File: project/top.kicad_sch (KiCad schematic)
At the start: 11 parts, among them J1 IDC 2x8, U1 top, U2 mag

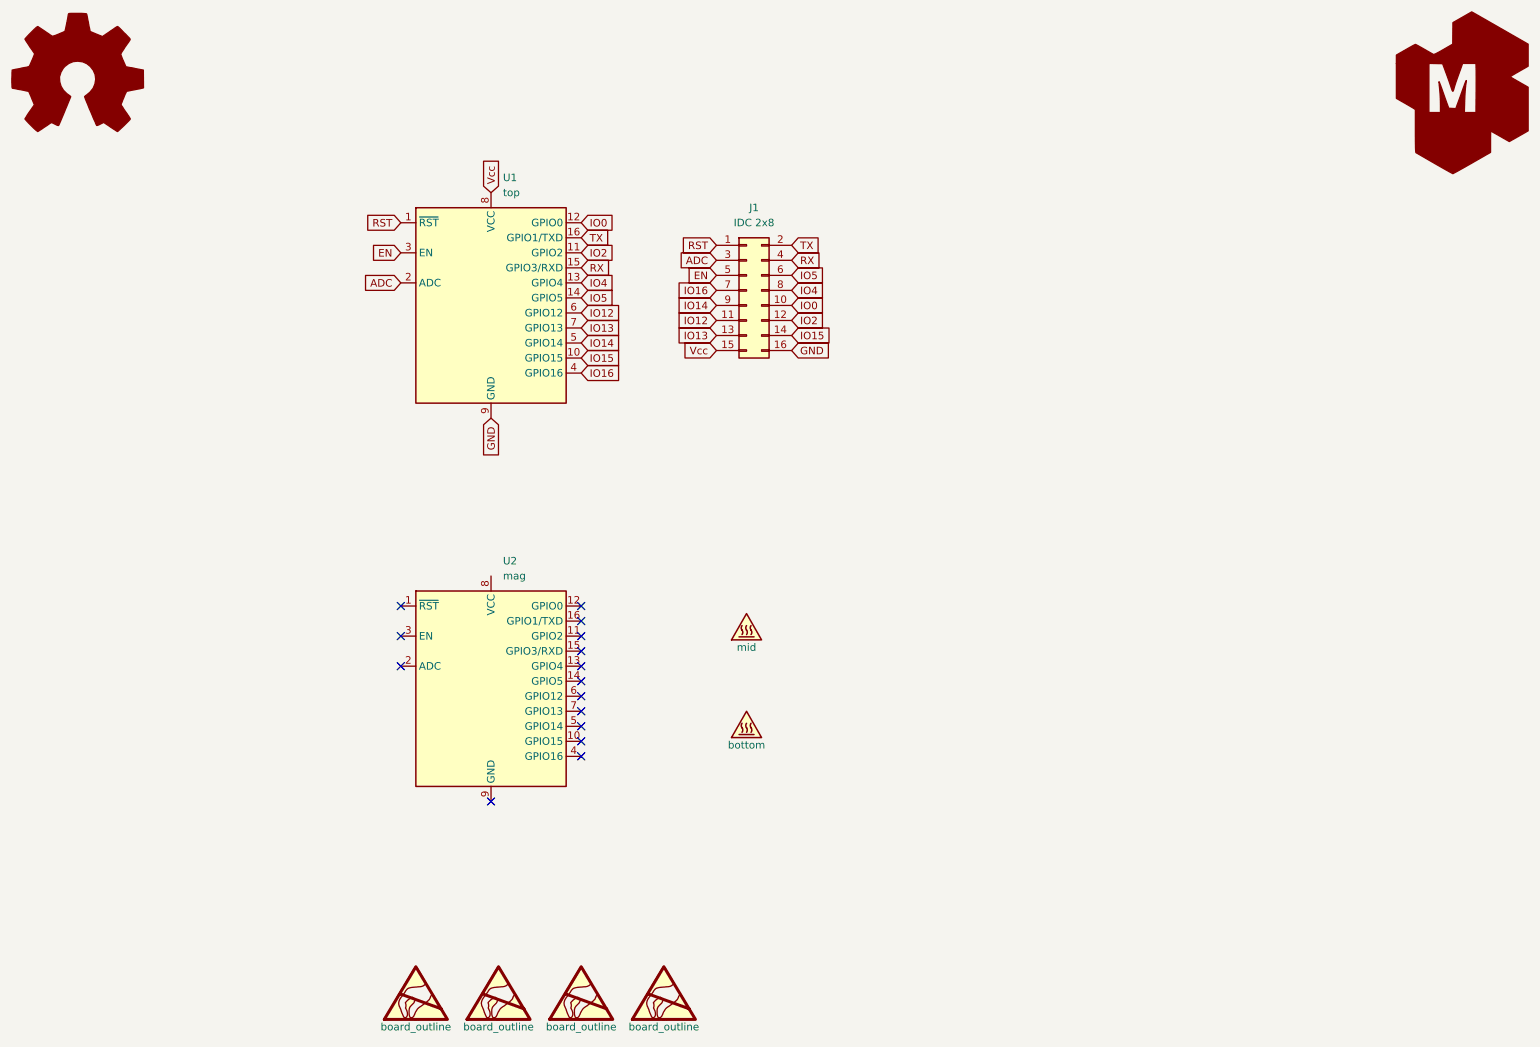
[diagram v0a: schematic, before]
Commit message: splitting boards into separate projects
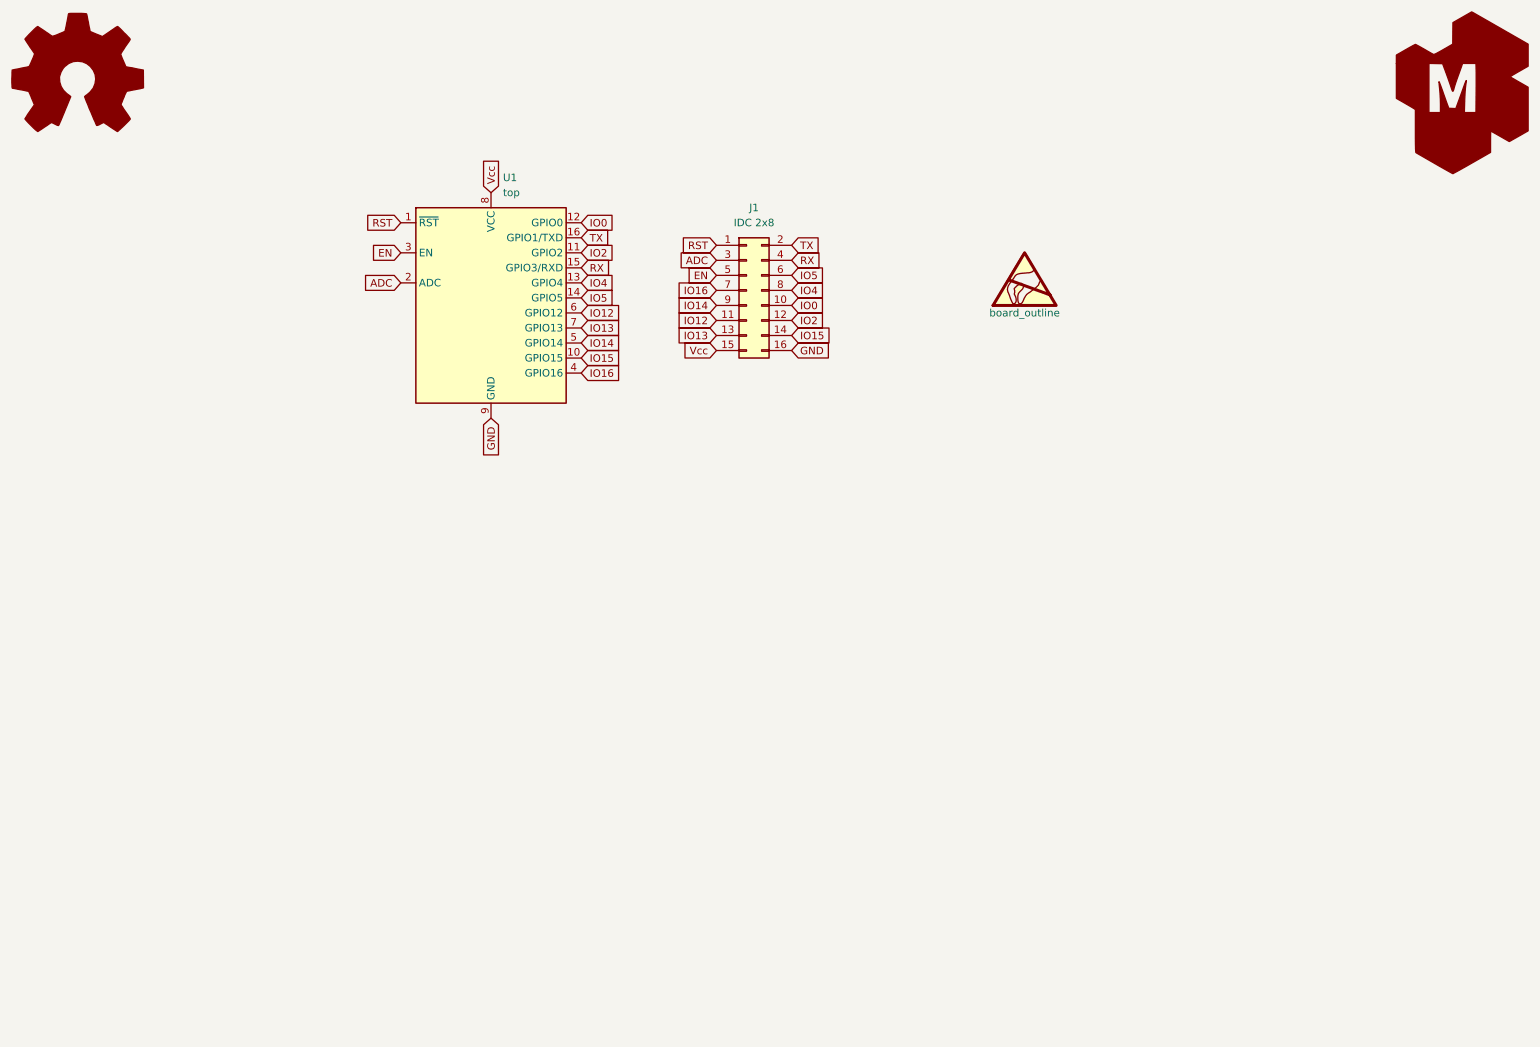
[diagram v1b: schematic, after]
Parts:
- removed SYM2, SYM3, SYM4: board_outline, -local:board, symbol Graphic:SYM_ESD_Large
- removed SYM5: mid, -local:esp-mid, symbol Graphic:SYM_Hot_Small
- removed SYM6: bottom, -local:esp-bottom, symbol Graphic:SYM_Hot_Small
- removed U2: mag, -local:esp-magnets, symbol RF_Module:ESP-07
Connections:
- no-connect marks 15 -> 0
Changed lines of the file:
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@@
     (company "makerspace.lt")
   )
-  (no_connect (at 115.57 121.92))
-  (no_connect (at 100.33 152.4))
-  (no_connect (at 115.57 124.46))
-  (no_connect (at 115.57 139.7))
-  (no_connect (at 115.57 137.16))
-  (no_connect (at 115.57 142.24))
-  (no_connect (at 85.09 124.46))
-  (no_connect (at 85.09 129.54))
-  (no_connect (at 115.57 119.38))
-  (no_connect (at 115.57 132.08))
-  (no_connect (at 115.57 127))
-  (no_connect (at 115.57 129.54))
-  (no_connect (at 115.57 134.62))
-  (no_connect (at 115.57 144.78))
-  (no_connect (at 85.09 119.38))
   (global_label "IO0" (shape input) (at 151.13 68.58 0) (fields_autoplaced)
     (effects (font (size 1.27 1.27)) (justify left))
@@
     (property "Intersheet References" "${INTERSHEET_REFS}" (id 0) (at 131.6626 73.7394 0)
       (effects (font (size 1.27 1.27)) (justify right) hide)
-    )
-  )
-  (symbol (lib_id "Graphic:SYM_ESD_Large") (at 101.6 184.15 0) (unit 1)
-    (in_bom no) (on_board yes) (fields_autoplaced)
-    (property "Reference" "SYM2" (id 0) (at 101.6 179.07 0)
-      (effects (font (size 1.27 1.27)) hide)
-    )
-    (property "Value" "board_outline" (id 1) (at 101.6 190.5 0))
-    (property "Footprint" "-local:board" (id 2) (at 101.473 184.912 0)
-      (effects (font (size 1.27 1.27)) hide)
-    )
-    (property "Datasheet" "~" (id 3) (at 101.473 184.912 0)
-      (effects (font (size 1.27 1.27)) hide)
     )
   )
@@
     (pin "9")
   )
-  (symbol (lib_id "Graphic:SYM_ESD_Large") (at 129.54 184.15 0) (unit 1)
+  (symbol (lib_id "Graphic:SYM_ESD_Large") (at 190.5 63.5 0) (unit 1)
     (in_bom no) (on_board yes) (fields_autoplaced)
-    (property "Reference" "SYM4" (id 0) (at 129.54 179.07 0)
-      (effects (font (size 1.27 1.27)) hide)
-    )
-    (property "Value" "board_outline" (id 1) (at 129.54 190.5 0))
-    (property "Footprint" "-local:board" (id 2) (at 129.413 184.912 0)
-      (effects (font (size 1.27 1.27)) hide)
-    )
-    (property "Datasheet" "~" (id 3) (at 129.413 184.912 0)
-      (effects (font (size 1.27 1.27)) hide)
-    )
-  )
-  (symbol (lib_id "Graphic:SYM_ESD_Large") (at 87.63 184.15 0) (unit 1)
+    (property "Reference" "SYM1" (id 0) (at 190.5 58.42 0)
+      (effects (font (size 1.27 1.27)) hide)
+    )
+    (property "Value" "board_outline" (id 1) (at 190.5 69.85 0))
+    (property "Footprint" "-local:board" (id 2) (at 190.373 64.262 0)
+      (effects (font (size 1.27 1.27)) hide)
+    )
+    (property "Datasheet" "~" (id 3) (at 190.373 64.262 0)
+      (effects (font (size 1.27 1.27)) hide)
+    )
+  )
+  (symbol (lib_id "RF_Module:ESP-07") (at 100.33 69.85 0) (unit 1)
     (in_bom no) (on_board yes) (fields_autoplaced)
-    (property "Reference" "SYM1" (id 0) (at 87.63 179.07 0)
-      (effects (font (size 1.27 1.27)) hide)
-    )
-    (property "Value" "board_outline" (id 1) (at 87.63 190.5 0))
-    (property "Footprint" "-local:board" (id 2) (at 87.503 184.912 0)
-      (effects (font (size 1.27 1.27)) hide)
-    )
-    (property "Datasheet" "~" (id 3) (at 87.503 184.912 0)
-      (effects (font (size 1.27 1.27)) hide)
-    )
-  )
-  (symbol (lib_id "RF_Module:ESP-07") (at 100.33 134.62 0) (unit 1)
-    (in_bom no) (on_board yes) (fields_autoplaced)
-    (property "Reference" "U2" (id 0) (at 102.3494 111.76 0)
+    (property "Reference" "U1" (id 0) (at 102.3494 46.99 0)
       (effects (font (size 1.27 1.27)) (justify left))
     )
-    (property "Value" "mag" (id 1) (at 102.3494 114.3 0)
+    (property "Value" "top" (id 1) (at 102.3494 49.53 0)
       (effects (font (size 1.27 1.27)) (justify left))
     )
-    (property "Footprint" "-local:esp-magnets" (id 2) (at 100.33 134.62 0)
-      (effects (font (size 1.27 1.27)) hide)
-    )
-    (property "Datasheet" "" (id 3) (at 91.44 132.08 0)
+    (property "Footprint" "-local:esp-top" (id 2) (at 100.33 69.85 0)
+      (effects (font (size 1.27 1.27)) hide)
+    )
+    (property "Datasheet" "" (id 3) (at 91.44 67.31 0)
       (effects (font (size 1.27 1.27)) hide)
     )
@@
     (pin "9")
   )
-  (symbol (lib_id "RF_Module:ESP-07") (at 100.33 69.85 0) (unit 1)
-    (in_bom no) (on_board yes) (fields_autoplaced)
-    (property "Reference" "U1" (id 0) (at 102.3494 46.99 0)
-      (effects (font (size 1.27 1.27)) (justify left))
-    )
-    (property "Value" "top" (id 1) (at 102.3494 49.53 0)
-      (effects (font (size 1.27 1.27)) (justify left))
-    )
-    (property "Footprint" "-local:esp-top" (id 2) (at 100.33 69.85 0)
-      (effects (font (size 1.27 1.27)) hide)
-    )
-    (property "Datasheet" "" (id 3) (at 91.44 67.31 0)
-      (effects (font (size 1.27 1.27)) hide)
-    )
-    (pin "1")
-    (pin "10")
-    (pin "11")
-    (pin "12")
-    (pin "13")
-    (pin "14")
-    (pin "15")
-    (pin "16")
-    (pin "2")
-    (pin "3")
-    (pin "4")
-    (pin "5")
-    (pin "6")
-    (pin "7")
-    (pin "8")
-    (pin "9")
-  )
   (symbol (lib_id "-local:LOGO_KMS") (at 262.89 31.75 0) (unit 1)
     (in_bom no) (on_board yes) (fields_autoplaced)
@@
     )
   )
-  (symbol (lib_id "Graphic:SYM_Hot_Small") (at 143.51 139.7 0) (unit 1)
-    (in_bom no) (on_board yes) (fields_autoplaced)
-    (property "Reference" "SYM6" (id 0) (at 143.51 136.144 0)
-      (effects (font (size 1.27 1.27)) hide)
-    )
-    (property "Value" "bottom" (id 1) (at 143.51 142.875 0))
-    (property "Footprint" "-local:esp-bottom" (id 2) (at 143.51 144.145 0)
-      (effects (font (size 1.27 1.27)) hide)
-    )
-    (property "Datasheet" "~" (id 3) (at 144.272 144.78 0)
-      (effects (font (size 1.27 1.27)) hide)
-    )
-  )
-  (symbol (lib_id "Graphic:SYM_ESD_Large") (at 115.57 184.15 0) (unit 1)
-    (in_bom no) (on_board yes) (fields_autoplaced)
-    (property "Reference" "SYM3" (id 0) (at 115.57 179.07 0)
-      (effects (font (size 1.27 1.27)) hide)
-    )
-    (property "Value" "board_outline" (id 1) (at 115.57 190.5 0))
-    (property "Footprint" "-local:board" (id 2) (at 115.443 184.912 0)
-      (effects (font (size 1.27 1.27)) hide)
-    )
-    (property "Datasheet" "~" (id 3) (at 115.443 184.912 0)
-      (effects (font (size 1.27 1.27)) hide)
-    )
-  )
-  (symbol (lib_id "Graphic:SYM_Hot_Small") (at 143.51 123.19 0) (unit 1)
-    (in_bom no) (on_board yes) (fields_autoplaced)
-    (property "Reference" "SYM5" (id 0) (at 143.51 119.634 0)
-      (effects (font (size 1.27 1.27)) hide)
-    )
-    (property "Value" "mid" (id 1) (at 143.51 126.365 0))
-    (property "Footprint" "-local:esp-mid" (id 2) (at 143.51 127.635 0)
-      (effects (font (size 1.27 1.27)) hide)
-    )
-    (property "Datasheet" "~" (id 3) (at 144.272 128.27 0)
-      (effects (font (size 1.27 1.27)) hide)
-    )
-  )
   (symbol (lib_id "Graphic:Logo_Open_Hardware_Large") (at 30.48 30.48 0) (unit 1)
-    (in_bom no) (on_board yes) (fields_autoplaced)
+    (in_bom no) (on_board no) (fields_autoplaced)
     (property "Reference" "G1" (id 0) (at 30.48 17.78 0)
       (effects (font (size 1.27 1.27)) hide)
@@
       (reference "SYM1") (unit 1) (value "board_outline") (footprint "-local:board")
     )
-    (path "/05faa11f-ae6d-468d-a3ec-adfec4991ea8"
-      (reference "SYM2") (unit 1) (value "board_outline") (footprint "-local:board")
-    )
-    (path "/b6bf8def-038e-46f8-896b-9a14af23a8be"
-      (reference "SYM3") (unit 1) (value "board_outline") (footprint "-local:board")
-    )
-    (path "/15281fb4-3d5f-4c1e-8f9a-028b9467b284"
-      (reference "SYM4") (unit 1) (value "board_outline") (footprint "-local:board")
-    )
-    (path "/b8de50e4-1c98-4df8-9118-d389fd142827"
-      (reference "SYM5") (unit 1) (value "mid") (footprint "-local:esp-mid")
-    )
-    (path "/7ebeb962-61f8-4540-8cdf-71658dedb14e"
-      (reference "SYM6") (unit 1) (value "bottom") (footprint "-local:esp-bottom")
-    )
     (path "/32a262a9-17d1-43be-ba01-da3c875db59b"
       (reference "U1") (unit 1) (value "top") (footprint "-local:esp-top")
     )
-    (path "/215c1653-c786-4754-a474-883213d8301e"
-      (reference "U2") (unit 1) (value "mag") (footprint "-local:esp-magnets")
-    )
-  )
+  )
